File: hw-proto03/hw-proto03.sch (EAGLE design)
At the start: 37 parts, among them IC1 TLV74333PDBVR, IC2 IR4427S, IC3 MCP2562T, IC5 IR4427S, J1 J15MM, J2 J5MM, J3 J12MM, J4 J5MM, Q1 SQJ147ELP-T1_GE3, Q2 SQJ147ELP-T1_GE3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

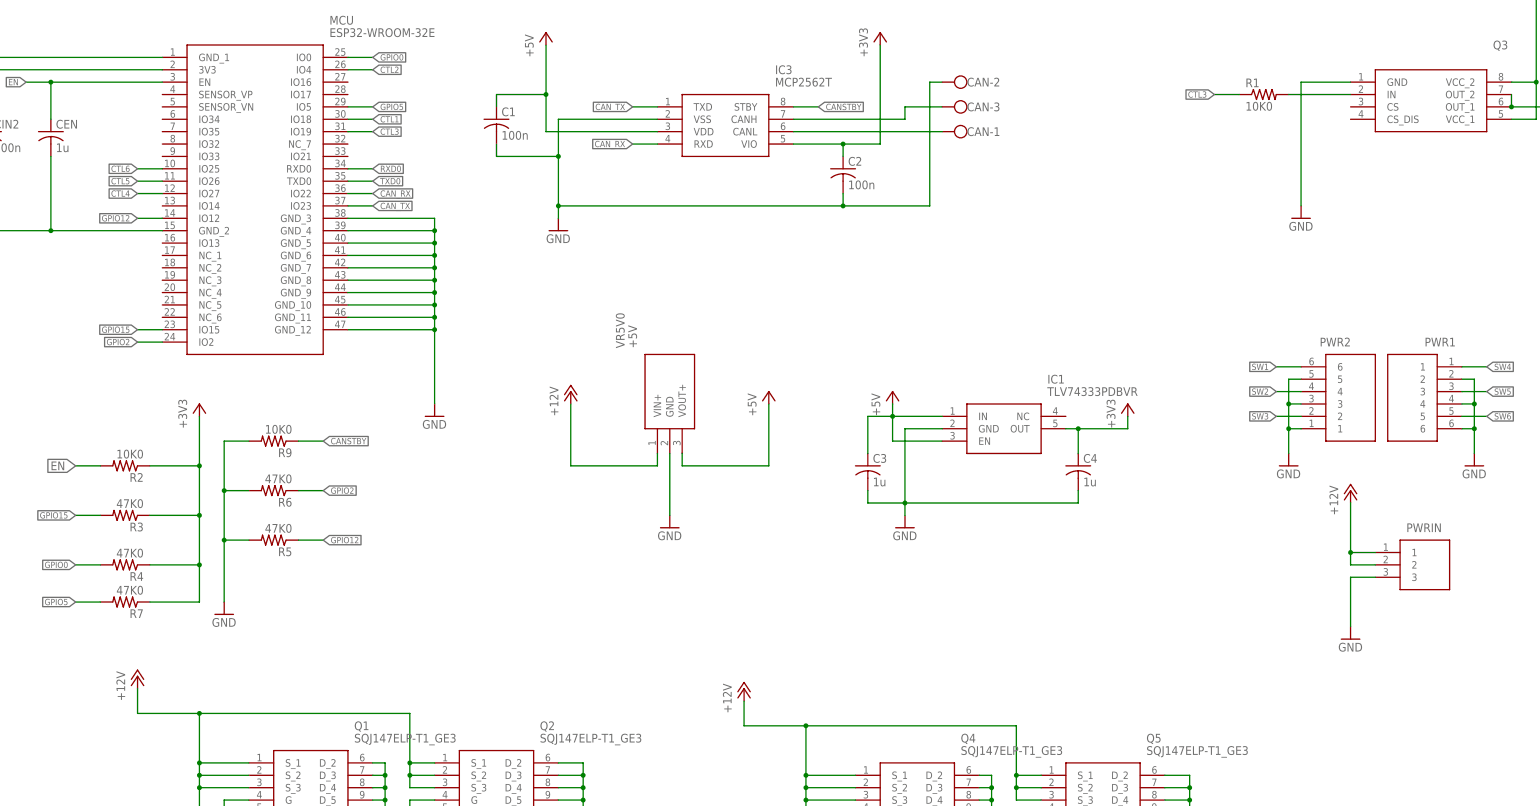
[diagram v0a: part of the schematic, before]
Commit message: layout refinement, added stiching
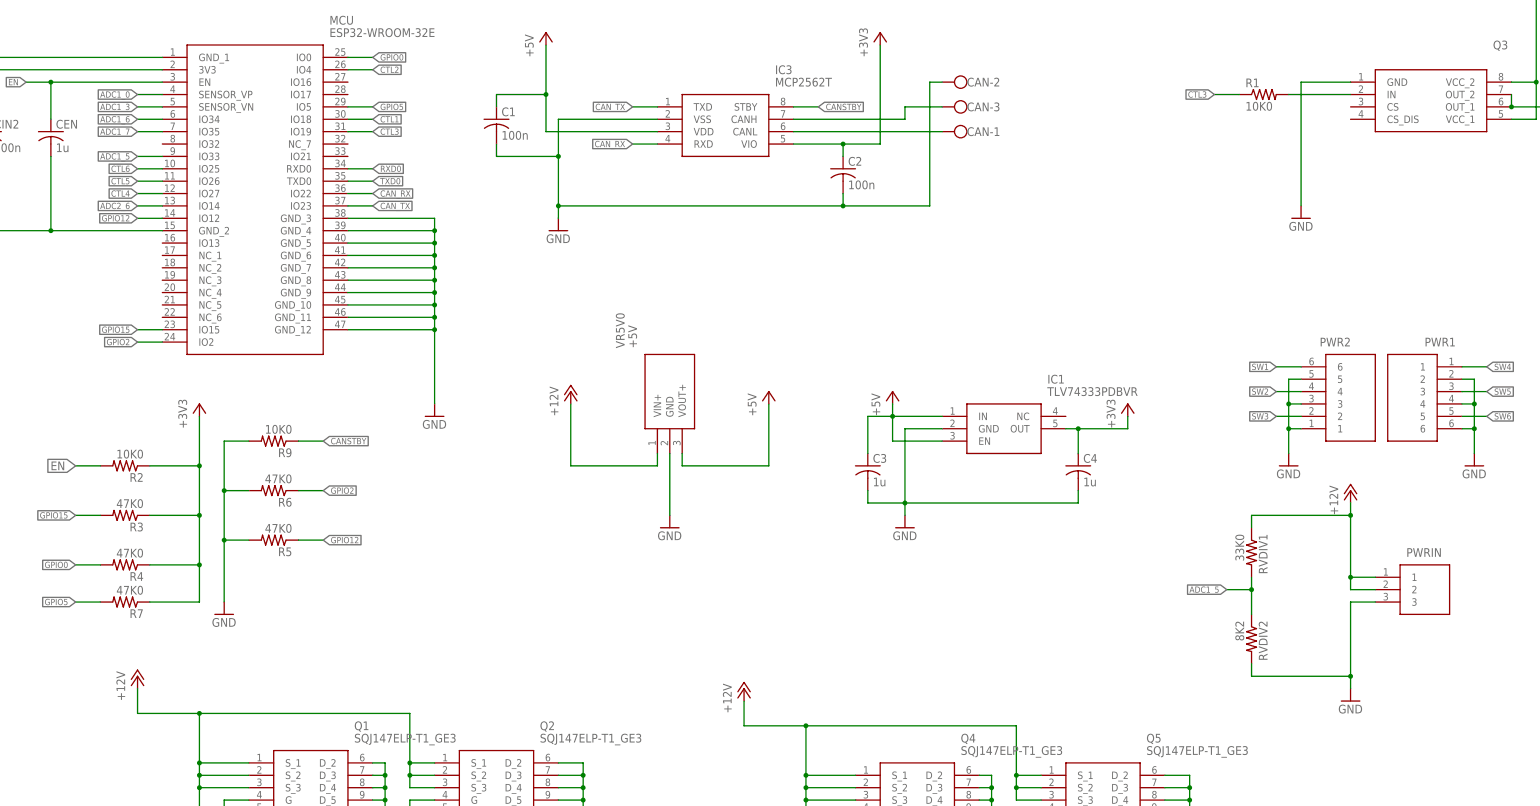
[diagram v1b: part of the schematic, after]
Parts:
- added RVDIV1: 33K0, rcl:R-US_R0603
- added RVDIV2: 8K2, rcl:R-US_R0603
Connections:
- new net ADC1_0: MCU.SENSOR_VP
- new net ADC1_3: MCU.SENSOR_VN
- new net ADC1_5: MCU.IO33, RVDIV1.2, RVDIV2.1
- new net ADC1_6: MCU.IO34
- new net ADC1_7: MCU.IO35
- new net ADC2_6: MCU.IO14
- net +12V: now also RVDIV1.1
- net GND: now also RVDIV2.2
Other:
- moved on the sheet: PWRIN
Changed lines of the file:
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@@
 <part name="C4" library="rcl" deviceset="C-US" device="C0603K" value="1u"/>
 <part name="R9" library="rcl" deviceset="R-US_" device="R0603" value="10K0"/>
+<part name="RVDIV1" library="rcl" deviceset="R-US_" device="R0603" value="33K0"/>
+<part name="RVDIV2" library="rcl" deviceset="R-US_" device="R0603" value="8K2"/>
 </parts>
 <sheets>
@@
 <instance part="GND2" gate="1" x="228.6" y="193.04"/>
 <instance part="GND5" gate="1" x="-60.96" y="152.4"/>
-<instance part="GND4" gate="1" x="238.76" y="106.68"/>
+<instance part="GND4" gate="1" x="238.76" y="93.98"/>
 <instance part="GND6" gate="1" x="76.2" y="190.5"/>
 <instance part="GND7" gate="1" x="147.32" y="129.54"/>
@@
 <instance part="Q5" gate="G$1" x="175.26" y="78.74"/>
 <instance part="GND12" gate="1" x="226.06" y="142.24"/>
-<instance part="PWRIN" gate="G$1" x="243.84" y="124.46" smashed="yes">
-<attribute name="NAME" x="250.19" y="129.54" size="1.778" layer="95" align="center-left"/>
-<attribute name="VALUE" x="260.35" y="129.54" size="1.778" layer="96" align="center-left"/>
+<instance part="PWRIN" gate="G$1" x="243.84" y="119.38" smashed="yes">
+<attribute name="NAME" x="250.19" y="124.46" size="1.778" layer="95" align="center-left"/>
+<attribute name="VALUE" x="260.35" y="124.46" size="1.778" layer="96" align="center-left"/>
 </instance>
 <instance part="PWR1" gate="G$1" x="261.62" y="162.56" smashed="yes" rot="MR0">
@@
 <instance part="C4" gate="G$1" x="182.88" y="142.24"/>
 <instance part="R9" gate="G$1" x="17.78" y="147.32" rot="R180"/>
+<instance part="RVDIV1" gate="G$1" x="218.44" y="124.46" rot="R270"/>
+<instance part="RVDIV2" gate="G$1" x="218.44" y="106.68" rot="R270"/>
 </instances>
 <busses>
@@
 <pinref part="PWRIN" gate="G$1" pin="3"/>
 <pinref part="GND4" gate="1" pin="GND"/>
-<wire x1="243.84" y1="119.38" x2="238.76" y2="119.38" width="0.1524" layer="91"/>
-<wire x1="238.76" y1="119.38" x2="238.76" y2="109.22" width="0.1524" layer="91"/>
+<wire x1="243.84" y1="114.3" x2="238.76" y2="114.3" width="0.1524" layer="91"/>
+<wire x1="238.76" y1="114.3" x2="238.76" y2="99.06" width="0.1524" layer="91"/>
+<pinref part="RVDIV2" gate="G$1" pin="2"/>
+<wire x1="238.76" y1="99.06" x2="238.76" y2="96.52" width="0.1524" layer="91"/>
+<wire x1="238.76" y1="99.06" x2="218.44" y2="99.06" width="0.1524" layer="91"/>
+<wire x1="218.44" y1="99.06" x2="218.44" y2="101.6" width="0.1524" layer="91"/>
+<junction x="238.76" y="99.06"/>
 </segment>
 <segment>
@@
 <pinref part="P+2" gate="1" pin="+12V"/>
 <pinref part="PWRIN" gate="G$1" pin="2"/>
-<wire x1="243.84" y1="121.92" x2="238.76" y2="121.92" width="0.1524" layer="91"/>
-<wire x1="238.76" y1="121.92" x2="238.76" y2="124.46" width="0.1524" layer="91"/>
+<wire x1="243.84" y1="116.84" x2="238.76" y2="116.84" width="0.1524" layer="91"/>
+<wire x1="238.76" y1="116.84" x2="238.76" y2="119.38" width="0.1524" layer="91"/>
 <pinref part="PWRIN" gate="G$1" pin="1"/>
-<wire x1="238.76" y1="124.46" x2="238.76" y2="134.62" width="0.1524" layer="91"/>
-<wire x1="243.84" y1="124.46" x2="238.76" y2="124.46" width="0.1524" layer="91"/>
-<junction x="238.76" y="124.46"/>
+<wire x1="238.76" y1="119.38" x2="238.76" y2="132.08" width="0.1524" layer="91"/>
+<wire x1="238.76" y1="132.08" x2="238.76" y2="134.62" width="0.1524" layer="91"/>
+<wire x1="243.84" y1="119.38" x2="238.76" y2="119.38" width="0.1524" layer="91"/>
+<junction x="238.76" y="119.38"/>
+<pinref part="RVDIV1" gate="G$1" pin="1"/>
+<wire x1="218.44" y1="129.54" x2="218.44" y2="132.08" width="0.1524" layer="91"/>
+<wire x1="218.44" y1="132.08" x2="238.76" y2="132.08" width="0.1524" layer="91"/>
+<junction x="238.76" y="132.08"/>
 </segment>
 <segment>
@@
 </segment>
 </net>
+<net name="ADC1_6" class="0">
+<segment>
+<pinref part="MCU" gate="G$1" pin="IO34"/>
+<wire x1="-10.16" y1="213.36" x2="-5.08" y2="213.36" width="0.1524" layer="91"/>
+<label x="-10.16" y="213.36" size="1.27" layer="95" rot="R180" xref="yes"/>
+</segment>
+</net>
+<net name="ADC1_7" class="0">
+<segment>
+<pinref part="MCU" gate="G$1" pin="IO35"/>
+<wire x1="-10.16" y1="210.82" x2="-5.08" y2="210.82" width="0.1524" layer="91"/>
+<label x="-10.16" y="210.82" size="1.27" layer="95" rot="R180" xref="yes"/>
+</segment>
+</net>
+<net name="ADC1_3" class="0">
+<segment>
+<pinref part="MCU" gate="G$1" pin="SENSOR_VN"/>
+<wire x1="-10.16" y1="215.9" x2="-5.08" y2="215.9" width="0.1524" layer="91"/>
+<label x="-10.16" y="215.9" size="1.27" layer="95" rot="R180" xref="yes"/>
+</segment>
+</net>
+<net name="ADC1_0" class="0">
+<segment>
+<pinref part="MCU" gate="G$1" pin="SENSOR_VP"/>
+<wire x1="-10.16" y1="218.44" x2="-5.08" y2="218.44" width="0.1524" layer="91"/>
+<label x="-10.16" y="218.44" size="1.27" layer="95" rot="R180" xref="yes"/>
+</segment>
+</net>
+<net name="ADC2_6" class="0">
+<segment>
+<pinref part="MCU" gate="G$1" pin="IO14"/>
+<wire x1="-10.16" y1="195.58" x2="-5.08" y2="195.58" width="0.1524" layer="91"/>
+<label x="-10.16" y="195.58" size="1.27" layer="95" rot="R180" xref="yes"/>
+</segment>
+</net>
+<net name="ADC1_5" class="0">
+<segment>
+<pinref part="MCU" gate="G$1" pin="IO33"/>
+<wire x1="-10.16" y1="205.74" x2="-5.08" y2="205.74" width="0.1524" layer="91"/>
+<label x="-10.16" y="205.74" size="1.27" layer="95" rot="R180" xref="yes"/>
+</segment>
+<segment>
+<pinref part="RVDIV2" gate="G$1" pin="1"/>
+<pinref part="RVDIV1" gate="G$1" pin="2"/>
+<wire x1="218.44" y1="111.76" x2="218.44" y2="116.84" width="0.1524" layer="91"/>
+<wire x1="218.44" y1="116.84" x2="218.44" y2="119.38" width="0.1524" layer="91"/>
+<wire x1="218.44" y1="116.84" x2="213.36" y2="116.84" width="0.1524" layer="91"/>
+<junction x="218.44" y="116.84"/>
+<label x="213.36" y="116.84" size="1.27" layer="95" rot="R180" xref="yes"/>
+</segment>
+</net>

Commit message: added passives, refined layout
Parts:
- added CIN3, CIN5: 100n, rcl:C-USC0603K
- added CIN4, CIN6: 4u7, rcl:C-USC0805K
- J1: value J15MM -> J12MM; device jumper:J15MM -> jumper:J12MM
- J4: value J5MM -> J7MM; device jumper:J5MM -> jumper:J7MM
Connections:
- net +12V: now also CIN3.1, CIN4.1, CIN5.1, CIN6.1
- net GND: now also CIN3.2, CIN4.2, CIN5.2, CIN6.2
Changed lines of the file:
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@@
 <grid distance="0.1" unitdist="inch" unit="inch" style="lines" multiple="1" display="no" altdistance="0.01" altunitdist="inch" altunit="inch"/>
 <layers>
-<layer number="1" name="Top" color="4" fill="1" visible="no" active="no"/>
-<layer number="16" name="Bottom" color="1" fill="1" visible="no" active="no"/>
-<layer number="17" name="Pads" color="2" fill="1" visible="no" active="no"/>
-<layer number="18" name="Vias" color="2" fill="1" visible="no" active="no"/>
-<layer number="19" name="Unrouted" color="6" fill="1" visible="no" active="no"/>
-<layer number="20" name="Dimension" color="15" fill="1" visible="no" active="no"/>
-<layer number="21" name="tPlace" color="7" fill="1" visible="no" active="no"/>
-<layer number="22" name="bPlace" color="7" fill="1" visible="no" active="no"/>
-<layer number="23" name="tOrigins" color="15" fill="1" visible="no" active="no"/>
-<layer number="24" name="bOrigins" color="15" fill="1" visible="no" active="no"/>
-<layer number="25" name="tNames" color="7" fill="1" visible="no" active="no"/>
-<layer number="26" name="bNames" color="7" fill="1" visible="no" active="no"/>
-<layer number="27" name="tValues" color="7" fill="1" visible="no" active="no"/>
-<layer number="28" name="bValues" color="7" fill="1" visible="no" active="no"/>
+<layer number="1" name="Top" color="4" fill="1" visible="yes" active="no"/>
+<layer number="16" name="Bottom" color="1" fill="1" visible="yes" active="no"/>
+<layer number="17" name="Pads" color="2" fill="1" visible="yes" active="no"/>
+<layer number="18" name="Vias" color="2" fill="1" visible="yes" active="no"/>
+<layer number="19" name="Unrouted" color="6" fill="1" visible="yes" active="no"/>
+<layer number="20" name="Dimension" color="15" fill="1" visible="yes" active="no"/>
+<layer number="21" name="tPlace" color="7" fill="1" visible="yes" active="no"/>
+<layer number="22" name="bPlace" color="7" fill="1" visible="yes" active="no"/>
+<layer number="23" name="tOrigins" color="15" fill="1" visible="yes" active="no"/>
+<layer number="24" name="bOrigins" color="15" fill="1" visible="yes" active="no"/>
+<layer number="25" name="tNames" color="7" fill="1" visible="yes" active="no"/>
+<layer number="26" name="bNames" color="7" fill="1" visible="yes" active="no"/>
+<layer number="27" name="tValues" color="7" fill="1" visible="yes" active="no"/>
+<layer number="28" name="bValues" color="7" fill="1" visible="yes" active="no"/>
 <layer number="29" name="tStop" color="7" fill="3" visible="no" active="no"/>
 <layer number="30" name="bStop" color="7" fill="6" visible="no" active="no"/>
@@
 <layer number="35" name="tGlue" color="7" fill="4" visible="no" active="no"/>
 <layer number="36" name="bGlue" color="7" fill="5" visible="no" active="no"/>
-<layer number="37" name="tTest" color="7" fill="1" visible="no" active="no"/>
-<layer number="38" name="bTest" color="7" fill="1" visible="no" active="no"/>
+<layer number="37" name="tTest" color="7" fill="1" visible="yes" active="no"/>
+<layer number="38" name="bTest" color="7" fill="1" visible="yes" active="no"/>
 <layer number="39" name="tKeepout" color="4" fill="11" visible="no" active="no"/>
 <layer number="40" name="bKeepout" color="1" fill="11" visible="no" active="no"/>
@@
 <layer number="44" name="Drills" color="7" fill="1" visible="no" active="no"/>
 <layer number="45" name="Holes" color="7" fill="1" visible="no" active="no"/>
-<layer number="46" name="Milling" color="3" fill="1" visible="no" active="no"/>
-<layer number="47" name="Measures" color="7" fill="1" visible="no" active="no"/>
-<layer number="48" name="Document" color="7" fill="1" visible="no" active="no"/>
-<layer number="49" name="Reference" color="7" fill="1" visible="no" active="no"/>
-<layer number="50" name="dxf" color="7" fill="1" visible="no" active="no"/>
-<layer number="51" name="tDocu" color="7" fill="1" visible="no" active="no"/>
-<layer number="52" name="bDocu" color="7" fill="1" visible="no" active="no"/>
-<layer number="53" name="tGND_GNDA" color="7" fill="9" visible="no" active="no"/>
-<layer number="54" name="bGND_GNDA" color="1" fill="9" visible="no" active="no"/>
-<layer number="56" name="wert" color="7" fill="1" visible="no" active="no"/>
-<layer number="57" name="tCAD" color="7" fill="1" visible="no" active="no"/>
-<layer number="59" name="tCarbon" color="7" fill="1" visible="no" active="no"/>
-<layer number="60" name="bCarbon" color="7" fill="1" visible="no" active="no"/>
+<layer number="46" name="Milling" color="3" fill="1" visible="yes" active="no"/>
+<layer number="47" name="Measures" color="7" fill="1" visible="yes" active="no"/>
+<layer number="48" name="Document" color="7" fill="1" visible="yes" active="no"/>
+<layer number="49" name="Reference" color="7" fill="1" visible="yes" active="no"/>
+<layer number="50" name="dxf" color="7" fill="1" visible="yes" active="no"/>
+<layer number="51" name="tDocu" color="7" fill="1" visible="yes" active="no"/>
+<layer number="52" name="bDocu" color="7" fill="1" visible="yes" active="no"/>
+<layer number="53" name="tGND_GNDA" color="7" fill="9" visible="yes" active="no"/>
+<layer number="54" name="bGND_GNDA" color="1" fill="9" visible="yes" active="no"/>
+<layer number="56" name="wert" color="7" fill="1" visible="yes" active="no"/>
+<layer number="57" name="tCAD" color="7" fill="1" visible="yes" active="no"/>
+<layer number="59" name="tCarbon" color="7" fill="1" visible="yes" active="no"/>
+<layer number="60" name="bCarbon" color="7" fill="1" visible="yes" active="no"/>
 <layer number="90" name="Modules" color="5" fill="1" visible="yes" active="yes"/>
 <layer number="91" name="Nets" color="2" fill="1" visible="yes" active="yes"/>
@@
 <part name="P+9" library="supply1" deviceset="+12V" device=""/>
 <part name="R8" library="rcl" deviceset="R-US_" device="0207/12" value="10K0"/>
-<part name="J1" library="jumper" deviceset="J" device="15MM" value="J15MM"/>
+<part name="J1" library="jumper" deviceset="J" device="12MM" value="J12MM"/>
 <part name="J2" library="jumper" deviceset="J" device="5MM"/>
 <part name="J3" library="jumper" deviceset="J" device="12MM" value="J12MM"/>
-<part name="J4" library="jumper" deviceset="J" device="5MM"/>
+<part name="J4" library="jumper" deviceset="J" device="7MM" value="J7MM"/>
 <part name="P+3" library="supply1" deviceset="+5V" device=""/>
 <part name="IC1" library="TLV74333PDBVR" deviceset="TLV74333PDBVR" device=""/>
@@
 <part name="RVDIV1" library="rcl" deviceset="R-US_" device="R0603" value="33K0"/>
 <part name="RVDIV2" library="rcl" deviceset="R-US_" device="R0603" value="8K2"/>
+<part name="CIN3" library="rcl" deviceset="C-US" device="C0603K" value="100n"/>
+<part name="CIN4" library="rcl" deviceset="C-US" device="C0805K" value="4u7"/>
+<part name="CIN5" library="rcl" deviceset="C-US" device="C0603K" value="100n"/>
+<part name="CIN6" library="rcl" deviceset="C-US" device="C0805K" value="4u7"/>
+<part name="GND15" library="supply1" deviceset="GND" device=""/>
+<part name="GND16" library="supply1" deviceset="GND" device=""/>
 </parts>
 <sheets>
@@
 <instance part="RVDIV1" gate="G$1" x="218.44" y="124.46" rot="R270"/>
 <instance part="RVDIV2" gate="G$1" x="218.44" y="106.68" rot="R270"/>
+<instance part="CIN3" gate="G$1" x="-10.16" y="78.74"/>
+<instance part="CIN4" gate="G$1" x="-20.32" y="78.74"/>
+<instance part="CIN5" gate="G$1" x="114.3" y="78.74"/>
+<instance part="CIN6" gate="G$1" x="104.14" y="78.74"/>
+<instance part="GND15" gate="1" x="-20.32" y="63.5"/>
+<instance part="GND16" gate="1" x="114.3" y="63.5"/>
 </instances>
 <busses>
@@
 <wire x1="317.5" y1="220.98" x2="317.5" y2="195.58" width="0.1524" layer="91"/>
 </segment>
+<segment>
+<pinref part="CIN4" gate="G$1" pin="2"/>
+<pinref part="GND15" gate="1" pin="GND"/>
+<wire x1="-20.32" y1="73.66" x2="-20.32" y2="71.12" width="0.1524" layer="91"/>
+<pinref part="CIN3" gate="G$1" pin="2"/>
+<wire x1="-20.32" y1="71.12" x2="-20.32" y2="66.04" width="0.1524" layer="91"/>
+<wire x1="-10.16" y1="73.66" x2="-10.16" y2="71.12" width="0.1524" layer="91"/>
+<wire x1="-10.16" y1="71.12" x2="-20.32" y2="71.12" width="0.1524" layer="91"/>
+<junction x="-20.32" y="71.12"/>
+</segment>
+<segment>
+<pinref part="CIN5" gate="G$1" pin="2"/>
+<pinref part="GND16" gate="1" pin="GND"/>
+<wire x1="114.3" y1="73.66" x2="114.3" y2="71.12" width="0.1524" layer="91"/>
+<pinref part="CIN6" gate="G$1" pin="2"/>
+<wire x1="114.3" y1="71.12" x2="114.3" y2="66.04" width="0.1524" layer="91"/>
+<wire x1="104.14" y1="73.66" x2="104.14" y2="71.12" width="0.1524" layer="91"/>
+<wire x1="104.14" y1="71.12" x2="114.3" y2="71.12" width="0.1524" layer="91"/>
+<junction x="114.3" y="71.12"/>
+</segment>
 </net>
 <net name="SW1" class="0">
@@
 <wire x1="45.72" y1="76.2" x2="45.72" y2="78.74" width="0.1524" layer="91"/>
 <junction x="45.72" y="78.74"/>
+<pinref part="CIN4" gate="G$1" pin="1"/>
+<wire x1="-20.32" y1="81.28" x2="-20.32" y2="83.82" width="0.1524" layer="91"/>
+<wire x1="-20.32" y1="83.82" x2="-10.16" y2="83.82" width="0.1524" layer="91"/>
+<wire x1="-10.16" y1="83.82" x2="-10.16" y2="91.44" width="0.1524" layer="91"/>
+<junction x="-10.16" y="91.44"/>
+<pinref part="CIN3" gate="G$1" pin="1"/>
+<wire x1="-10.16" y1="81.28" x2="-10.16" y2="83.82" width="0.1524" layer="91"/>
+<junction x="-10.16" y="83.82"/>
 </segment>
 <segment>
@@
 <wire x1="170.18" y1="73.66" x2="170.18" y2="76.2" width="0.1524" layer="91"/>
 <junction x="170.18" y="76.2"/>
-</segment>
-<segment>
+<pinref part="CIN6" gate="G$1" pin="1"/>
+<wire x1="104.14" y1="81.28" x2="104.14" y2="83.82" width="0.1524" layer="91"/>
+<wire x1="104.14" y1="83.82" x2="114.3" y2="83.82" width="0.1524" layer="91"/>
+<wire x1="114.3" y1="83.82" x2="114.3" y2="88.9" width="0.1524" layer="91"/>
+<junction x="114.3" y="88.9"/>
+<pinref part="CIN5" gate="G$1" pin="1"/>
+<wire x1="114.3" y1="81.28" x2="114.3" y2="83.82" width="0.1524" layer="91"/>
+<junction x="114.3" y="83.82"/>
+</segment>
+<segment>
